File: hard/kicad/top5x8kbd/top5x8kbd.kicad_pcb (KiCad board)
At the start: 2 copper layers, 177.8 x 130.8 mm, 77 parts, among them J1 EXPANSION, J2 TO COMPUTER, J23 DB9_Male, J44 DB9_Male, J5 TO COMPUTER (DIRECT), SW1 1 !, SW10 0 _, SW11 Q ¡, SW12 W ~~, SW13 E é, SW14 R <, SW15 T >, SW16 Y ü, SW17 U ú, SW18 I í, SW19 O ó, SW2 2 @, SW20 P ", SW21 A á, SW22 S ;, SW23 D |, SW24 F [, SW25 G ], SW26 H ^, SW27 J -, SW28 K +, SW29 L =, SW3 3 #, SW30 ENTER ñ, SW31 SHIFT, SW32 Z :, SW33 X ¿, SW34 C ?, SW35 V /, SW36 B *, SW37 N ,, SW38 M ., SW39 ALT, SW4 4 $, SW40 SPACE, SW5 5 %, SW6 6 &, SW7 7 ', SW8 8 (, SW9 9 (, U1 74HC138, U12 74HC174, U13 74HC245, U24 74HC245, U26 74HC174, U34 74HC595, U45 74HC245, U55 74HC595, U9 74HC86

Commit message: add Sinclair keyboard headers
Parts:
- added J16: COLUMN, Connector_PinSocket_2.54mm:PinSocket_1x05_P2.54mm_Vertical, F.Cu at (135.9, 80.0)
- added J17: ROW, Connector_PinSocket_2.54mm:PinSocket_1x08_P2.54mm_Vertical, F.Cu at (153.7, 80.0)
- H3, H4, H5, H6, H7, H8: value MountingHole -> (none)
- LOGO1, LOGO2, LOGO3: value Logo_Open_Hardware_Large -> (none)
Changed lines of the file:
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@@
     (tracks 0)
     (zones 0)
-    (modules 77)
+    (modules 79)
     (nets 50)
   )
@@
     (add_net ROW8)
   )
+  (module Connector_PinSocket_2.54mm:PinSocket_1x08_P2.54mm_Vertical (layer F.Cu)
+    (at 153.67 80.01 90)
+    (descr "Through hole straight socket strip, 1x08, 2.54mm pitch, single row (from Kicad 4.0.7), script generated")
+    (tags "Through hole socket strip THT 1x08 2.54mm single row")
+    (fp_text reference J17 (at 2.54 8.89 unlocked) (layer B.SilkS)
+      (effects (font (size 1 1) (thickness 0.15)) (justify mirror))
+    )
+    (fp_text value ROW (at 2.54 8.89 180) (layer F.Fab)
+      (effects (font (size 1 1) (thickness 0.15)))
+    )
+    (fp_text user %R (at 0 8.89) (layer F.Fab)
+      (effects (font (size 1 1) (thickness 0.15)))
+    )
+    (fp_line (start -1.8 19.55) (end -1.8 -1.8) (layer F.CrtYd) (width 0.05))
+    (fp_line (start 1.75 19.55) (end -1.8 19.55) (layer F.CrtYd) (width 0.05))
+    (fp_line (start 1.75 -1.8) (end 1.75 19.55) (layer F.CrtYd) (width 0.05))
+    (fp_line (start -1.8 -1.8) (end 1.75 -1.8) (layer F.CrtYd) (width 0.05))
+    (fp_line (start 0 -1.33) (end 1.33 -1.33) (layer F.SilkS) (width 0.12))
+    (fp_line (start 1.33 -1.33) (end 1.33 0) (layer F.SilkS) (width 0.12))
+    (fp_line (start 1.33 1.27) (end 1.33 19.11) (layer F.SilkS) (width 0.12))
+    (fp_line (start -1.33 19.11) (end 1.33 19.11) (layer F.SilkS) (width 0.12))
+    (fp_line (start -1.33 1.27) (end -1.33 19.11) (layer F.SilkS) (width 0.12))
+    (fp_line (start -1.33 1.27) (end 1.33 1.27) (layer F.SilkS) (width 0.12))
+    (fp_line (start -1.27 19.05) (end -1.27 -1.27) (layer F.Fab) (width 0.1))
+    (fp_line (start 1.27 19.05) (end -1.27 19.05) (layer F.Fab) (width 0.1))
+    (fp_line (start 1.27 -0.635) (end 1.27 19.05) (layer F.Fab) (width 0.1))
+    (fp_line (start 0.635 -1.27) (end 1.27 -0.635) (layer F.Fab) (width 0.1))
+    (fp_line (start -1.27 -1.27) (end 0.635 -1.27) (layer F.Fab) (width 0.1))
+    (pad 8 thru_hole oval (at 0 17.78 90) (size 1.7 1.7) (drill 1) (layers *.Cu *.Mask)
+      (net 14 ROW8))
+    (pad 7 thru_hole oval (at 0 15.24 90) (size 1.7 1.7) (drill 1) (layers *.Cu *.Mask)
+      (net 12 ROW7))
+    (pad 6 thru_hole oval (at 0 12.7 90) (size 1.7 1.7) (drill 1) (layers *.Cu *.Mask)
+      (net 13 ROW6))
+    (pad 5 thru_hole oval (at 0 10.16 90) (size 1.7 1.7) (drill 1) (layers *.Cu *.Mask)
+      (net 10 ROW5))
+    (pad 4 thru_hole oval (at 0 7.62 90) (size 1.7 1.7) (drill 1) (layers *.Cu *.Mask)
+      (net 11 ROW3))
+    (pad 3 thru_hole oval (at 0 5.08 90) (size 1.7 1.7) (drill 1) (layers *.Cu *.Mask)
+      (net 8 ROW4))
+    (pad 2 thru_hole oval (at 0 2.54 90) (size 1.7 1.7) (drill 1) (layers *.Cu *.Mask)
+      (net 9 ROW2))
+    (pad 1 thru_hole rect (at 0 0 90) (size 1.7 1.7) (drill 1) (layers *.Cu *.Mask)
+      (net 3 ROW1))
+    (model ${KISYS3DMOD}/Connector_PinSocket_2.54mm.3dshapes/PinSocket_1x08_P2.54mm_Vertical.wrl
+      (at (xyz 0 0 0))
+      (scale (xyz 1 1 1))
+      (rotate (xyz 0 0 0))
+    )
+  )
+  (module Connector_PinSocket_2.54mm:PinSocket_1x05_P2.54mm_Vertical (layer F.Cu)
+    (at 135.89 80.01 90)
+    (descr "Through hole straight socket strip, 1x05, 2.54mm pitch, single row (from Kicad 4.0.7), script generated")
+    (tags "Through hole socket strip THT 1x05 2.54mm single row")
+    (fp_text reference J16 (at 2.54 5.08 unlocked) (layer B.SilkS)
+      (effects (font (size 1 1) (thickness 0.15)) (justify mirror))
+    )
+    (fp_text value COLUMN (at 2.54 5.08) (layer F.Fab)
+      (effects (font (size 1 1) (thickness 0.15)))
+    )
+    (fp_text user %R (at 0 5.08) (layer F.Fab)
+      (effects (font (size 1 1) (thickness 0.15)))
+    )
+    (fp_line (start -1.8 11.9) (end -1.8 -1.8) (layer F.CrtYd) (width 0.05))
+    (fp_line (start 1.75 11.9) (end -1.8 11.9) (layer F.CrtYd) (width 0.05))
+    (fp_line (start 1.75 -1.8) (end 1.75 11.9) (layer F.CrtYd) (width 0.05))
+    (fp_line (start -1.8 -1.8) (end 1.75 -1.8) (layer F.CrtYd) (width 0.05))
+    (fp_line (start 0 -1.33) (end 1.33 -1.33) (layer F.SilkS) (width 0.12))
+    (fp_line (start 1.33 -1.33) (end 1.33 0) (layer F.SilkS) (width 0.12))
+    (fp_line (start 1.33 1.27) (end 1.33 11.49) (layer F.SilkS) (width 0.12))
+    (fp_line (start -1.33 11.49) (end 1.33 11.49) (layer F.SilkS) (width 0.12))
+    (fp_line (start -1.33 1.27) (end -1.33 11.49) (layer F.SilkS) (width 0.12))
+    (fp_line (start -1.33 1.27) (end 1.33 1.27) (layer F.SilkS) (width 0.12))
+    (fp_line (start -1.27 11.43) (end -1.27 -1.27) (layer F.Fab) (width 0.1))
+    (fp_line (start 1.27 11.43) (end -1.27 11.43) (layer F.Fab) (width 0.1))
+    (fp_line (start 1.27 -0.635) (end 1.27 11.43) (layer F.Fab) (width 0.1))
+    (fp_line (start 0.635 -1.27) (end 1.27 -0.635) (layer F.Fab) (width 0.1))
+    (fp_line (start -1.27 -1.27) (end 0.635 -1.27) (layer F.Fab) (width 0.1))
+    (pad 5 thru_hole oval (at 0 10.16 90) (size 1.7 1.7) (drill 1) (layers *.Cu *.Mask)
+      (net 7 COL5))
+    (pad 4 thru_hole oval (at 0 7.62 90) (size 1.7 1.7) (drill 1) (layers *.Cu *.Mask)
+      (net 6 COL4))
+    (pad 3 thru_hole oval (at 0 5.08 90) (size 1.7 1.7) (drill 1) (layers *.Cu *.Mask)
+      (net 5 COL3))
+    (pad 2 thru_hole oval (at 0 2.54 90) (size 1.7 1.7) (drill 1) (layers *.Cu *.Mask)
+      (net 4 COL2))
+    (pad 1 thru_hole rect (at 0 0 90) (size 1.7 1.7) (drill 1) (layers *.Cu *.Mask)
+      (net 2 COL1))
+    (model ${KISYS3DMOD}/Connector_PinSocket_2.54mm.3dshapes/PinSocket_1x05_P2.54mm_Vertical.wrl
+      (at (xyz 0 0 0))
+      (scale (xyz 1 1 1))
+      (rotate (xyz 0 0 0))
+    )
+  )
   (module Jumper:SolderJumper-3_P1.3mm_Open_RoundedPad1.0x1.5mm (layer F.Cu)
     (at 162.56 45.72)
@@
       (effects (font (size 1.524 1.524) (thickness 0.3)))
     )
-    (fp_text value Logo_Open_Hardware_Large (at 0.75 0) (layer F.SilkS) hide
+    (fp_text value " " (at 0.75 0) (layer F.SilkS) hide
       (effects (font (size 1.524 1.524) (thickness 0.3)))
     )
@@
       (effects (font (size 1.524 1.524) (thickness 0.3)))
     )
-    (fp_text value Logo_Open_Hardware_Large (at 0.75 0) (layer F.SilkS) hide
+    (fp_text value " " (at 0.75 0) (layer F.SilkS) hide
       (effects (font (size 1.524 1.524) (thickness 0.3)))
     )
@@
       (effects (font (size 1 1) (thickness 0.15)))
     )
-    (fp_text value Logo_Open_Hardware_Large (at 0.75 0) (layer F.Fab) hide
+    (fp_text value " " (at 0.75 0) (layer F.Fab) hide
       (effects (font (size 1 1) (thickness 0.15)))
     )
@@
       (effects (font (size 1 1) (thickness 0.15)))
     )
-    (fp_text value MountingHole (at 0 3.8) (layer F.Fab)
+    (fp_text value " " (at 0 3.8) (layer F.Fab)
       (effects (font (size 1 1) (thickness 0.15)))
     )
@@
       (effects (font (size 1 1) (thickness 0.15)))
     )
-    (fp_text value MountingHole (at 0 3.8) (layer F.Fab)
+    (fp_text value " " (at 0 3.8) (layer F.Fab)
       (effects (font (size 1 1) (thickness 0.15)))
     )
@@
       (effects (font (size 1 1) (thickness 0.15)))
     )
-    (fp_text value MountingHole (at 0 3.8) (layer F.Fab)
+    (fp_text value " " (at 0 3.8) (layer F.Fab)
       (effects (font (size 1 1) (thickness 0.15)))
     )
@@
       (effects (font (size 1 1) (thickness 0.15)))
     )
-    (fp_text value MountingHole (at 0 3.8) (layer F.Fab)
+    (fp_text value " " (at 0 3.8) (layer F.Fab)
       (effects (font (size 1 1) (thickness 0.15)))
     )
@@
       (effects (font (size 1 1) (thickness 0.15)))
     )
-    (fp_text value MountingHole (at 0 3.8) (layer F.Fab)
+    (fp_text value " " (at 0 3.8) (layer F.Fab)
       (effects (font (size 1 1) (thickness 0.15)))
     )
@@
       (effects (font (size 1 1) (thickness 0.15)))
     )
-    (fp_text value MountingHole (at 0 3.8) (layer F.Fab)
+    (fp_text value " " (at 0 3.8) (layer F.Fab)
       (effects (font (size 1 1) (thickness 0.15)))
     )
@@
     (fp_line (start 6.25 -0.75) (end 6.25 5.25) (layer F.Fab) (width 0.1))
     (fp_line (start 3.25 -0.75) (end 6.25 -0.75) (layer F.Fab) (width 0.1))
-    (fp_text user %R (at 3.25 2.25) (layer F.Fab)
-      (effects (font (size 1 1) (thickness 0.15)))
-    )
+    (fp_text user BREAK (at 3.175 8.89) (layer F.SilkS)
+      (effects (font (size 1 1) (thickness 0.15)))
+    )

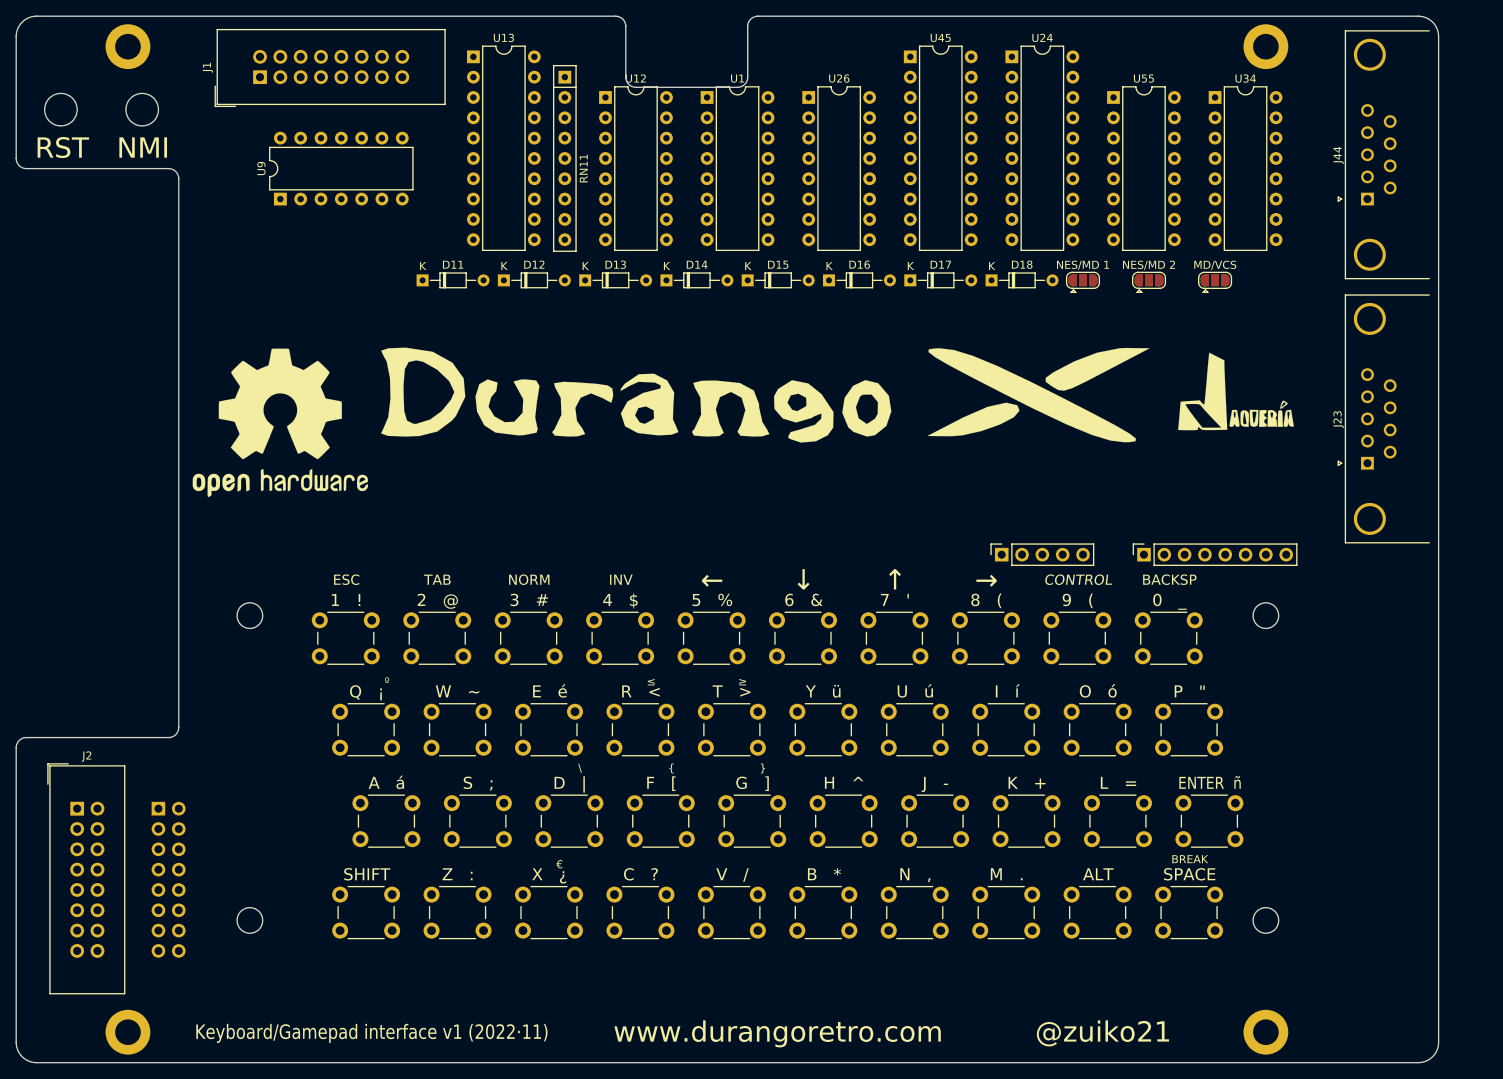
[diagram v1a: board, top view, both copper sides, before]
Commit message: fix cover edge cuts
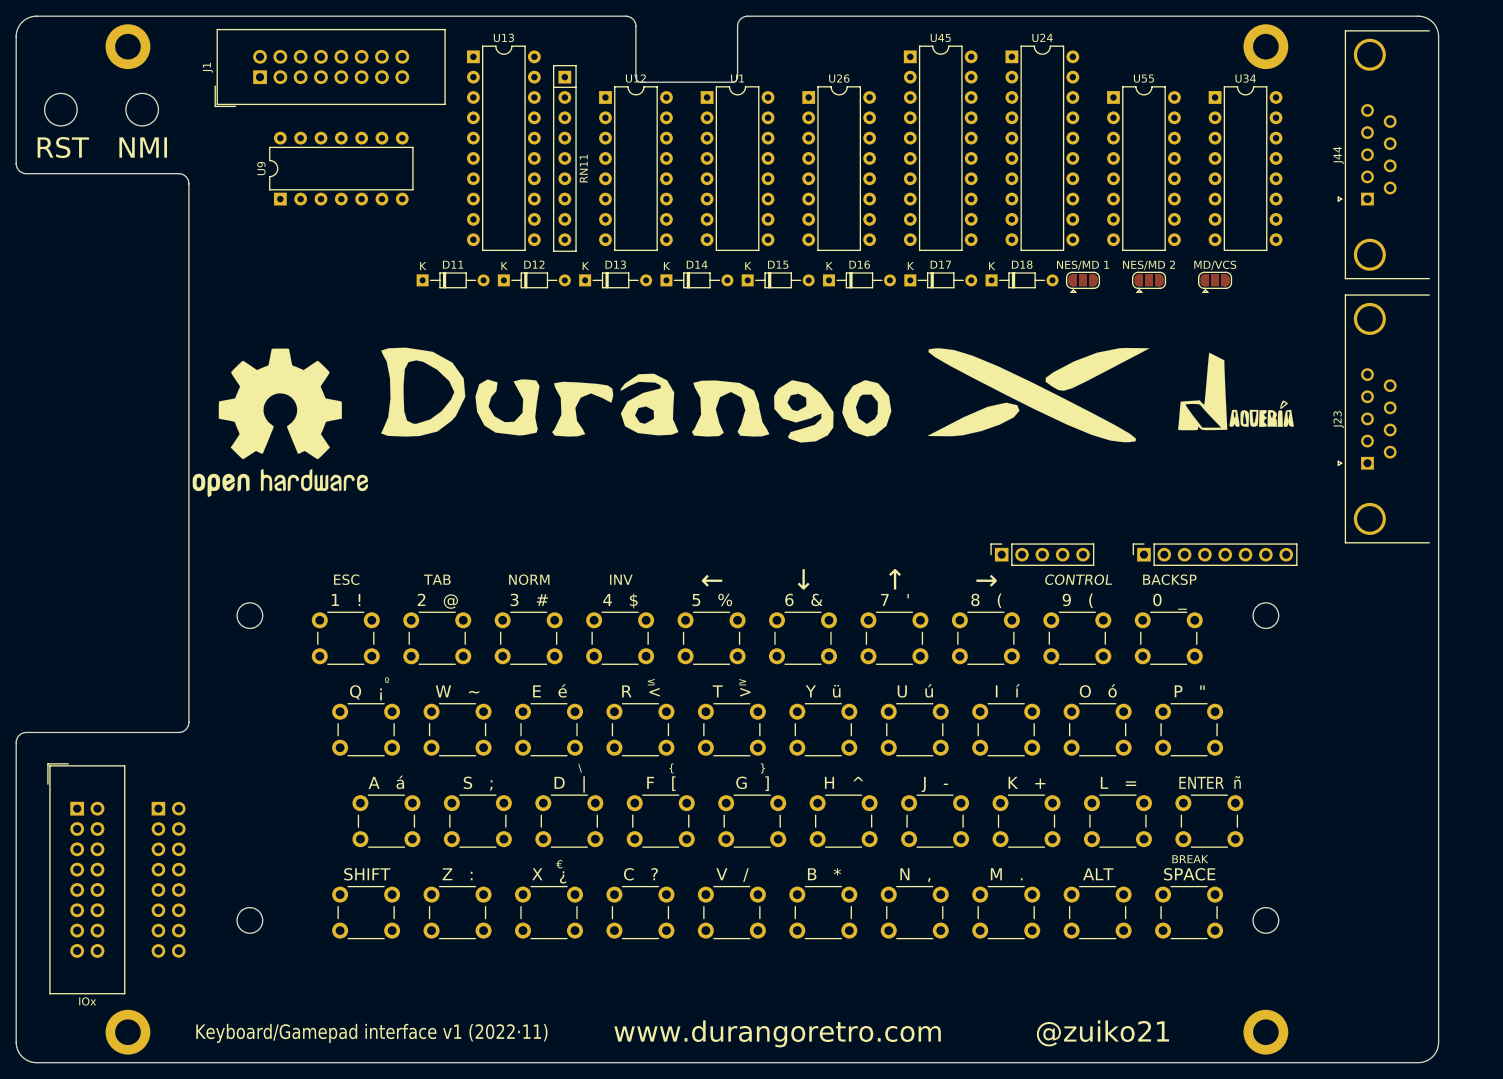
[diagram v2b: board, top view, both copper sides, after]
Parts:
- J1: value EXPANSION -> IOx
- J2: value TO COMPUTER -> IOx
- J5: value TO COMPUTER (DIRECT) -> TO COMPUTER
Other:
- outline, holes or cut-outs redrawn
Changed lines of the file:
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@@
       (effects (font (size 1 1) (thickness 0.15)) (justify mirror))
     )
-    (fp_text value "TO COMPUTER (DIRECT)" (at -1.27 -20.55) (layer B.Fab)
-      (effects (font (size 1 1) (thickness 0.15)) (justify mirror))
-    )
-    (fp_text user %R (at -1.27 -8.89 270) (layer B.Fab)
+    (fp_text value "TO COMPUTER" (at -1.27 -20.55 unlocked) (layer B.SilkS)
       (effects (font (size 1 1) (thickness 0.15)) (justify mirror))
     )
@@
     (descr "Through hole straight IDC box header, 2x08, 2.54mm pitch, double rows")
     (tags "Through hole IDC box header THT 2x08 2.54mm double row")
-    (fp_text reference J2 (at 1.27 -6.604) (layer F.SilkS)
-      (effects (font (size 1 1) (thickness 0.15)))
+    (fp_text reference J2 (at 1.27 -1.905 unlocked) (layer B.SilkS)
+      (effects (font (size 1 1) (thickness 0.15)) (justify mirror))
     )
-    (fp_text value "TO COMPUTER" (at 1.27 24.384) (layer F.Fab)
+    (fp_text value IOx (at 1.27 24.13 unlocked) (layer F.SilkS)
       (effects (font (size 1 1) (thickness 0.15)))
     )
@@
     (fp_line (start 5.145 -4.56) (end 5.145 22.32) (layer F.Fab) (width 0.1))
     (fp_line (start 5.695 -5.1) (end 5.695 22.88) (layer F.Fab) (width 0.1))
-    (fp_text user %R (at 1.27 8.89) (layer F.Fab)
-      (effects (font (size 1 1) (thickness 0.15)))
-    )
     (pad 16 thru_hole oval (at 2.54 17.78) (size 1.7272 1.7272) (drill 1.016) (layers *.Cu *.Mask)
       (net 15 PD7))
@@
       (effects (font (size 1 1) (thickness 0.15)))
     )
-    (fp_text value EXPANSION (at 1.27 24.384 90) (layer F.Fab)
+    (fp_text value IOx (at 1.27 24.384 90) (layer F.Fab)
       (effects (font (size 1 1) (thickness 0.15)))
     )
@@
     )
   )
+  (gr_arc (start 102.235 20.32) (end 102.235 20.955) (angle -90) (layer Edge.Cuts) (width 0.05))
+  (gr_arc (start 90.805 20.32) (end 90.17 20.32) (angle -90) (layer Edge.Cuts) (width 0.05))
   (gr_text @zuiko21 (at 148.59 139.7) (layer F.SilkS)
     (effects (font (size 2.54 2.54) (thickness 0.45)))
@@
     (effects (font (size 2.54 2.54) (thickness 0.3)))
   )
-  (gr_line (start 88.9 13.97) (end 88.9 20.32) (layer Edge.Cuts) (width 0.05))
-  (gr_arc (start 105.41 13.97) (end 105.41 12.7) (angle -90) (layer Edge.Cuts) (width 0.05))
-  (gr_arc (start 102.87 20.32) (end 102.87 21.59) (angle -90) (layer Edge.Cuts) (width 0.05))
-  (gr_arc (start 90.17 20.32) (end 88.9 20.32) (angle -90) (layer Edge.Cuts) (width 0.05))
-  (gr_line (start 105.41 12.7) (end 187.96 12.7) (layer Edge.Cuts) (width 0.05))
-  (gr_line (start 104.14 20.32) (end 104.14 13.97) (layer Edge.Cuts) (width 0.05))
-  (gr_line (start 90.17 21.59) (end 102.87 21.59) (layer Edge.Cuts) (width 0.05))
-  (gr_arc (start 87.63 13.97) (end 88.9 13.97) (angle -90) (layer Edge.Cuts) (width 0.05))
+  (gr_line (start 90.17 13.97) (end 90.17 20.32) (layer Edge.Cuts) (width 0.05))
+  (gr_arc (start 104.14 13.97) (end 104.14 12.7) (angle -90) (layer Edge.Cuts) (width 0.05))
+  (gr_line (start 104.14 12.7) (end 187.96 12.7) (layer Edge.Cuts) (width 0.05))
+  (gr_line (start 102.87 20.32) (end 102.87 13.97) (layer Edge.Cuts) (width 0.05))
+  (gr_line (start 90.805 20.955) (end 102.235 20.955) (layer Edge.Cuts) (width 0.05))
+  (gr_arc (start 88.9 13.97) (end 90.17 13.97) (angle -90) (layer Edge.Cuts) (width 0.05))
   (gr_circle (center 28.448 24.384) (end 30.48 24.384) (layer Edge.Cuts) (width 0.12))
   (gr_circle (center 18.288 24.384) (end 20.32 24.384) (layer Edge.Cuts) (width 0.12))
-  (gr_arc (start 13.97 104.14) (end 13.97 102.87) (angle -90) (layer Edge.Cuts) (width 0.05))
-  (gr_arc (start 31.75 101.6) (end 31.75 102.87) (angle -90) (layer Edge.Cuts) (width 0.05))
-  (gr_arc (start 31.75 33.02) (end 33.02 33.02) (angle -90) (layer Edge.Cuts) (width 0.05))
-  (gr_arc (start 13.97 30.48) (end 12.7 30.48) (angle -90) (layer Edge.Cuts) (width 0.05))
+  (gr_arc (start 13.97 103.505) (end 13.97 102.235) (angle -90) (layer Edge.Cuts) (width 0.05))
+  (gr_arc (start 33.02 100.965) (end 33.02 102.235) (angle -90) (layer Edge.Cuts) (width 0.05))
+  (gr_arc (start 33.02 33.655) (end 34.29 33.655) (angle -90) (layer Edge.Cuts) (width 0.05))
+  (gr_arc (start 13.97 31.115) (end 12.7 31.115) (angle -90) (layer Edge.Cuts) (width 0.05))
   (gr_arc (start 15.24 140.97) (end 12.7 140.97) (angle -90) (layer Edge.Cuts) (width 0.05))
   (gr_arc (start 187.96 140.97) (end 187.96 143.51) (angle -90) (layer Edge.Cuts) (width 0.05))
   (gr_arc (start 187.96 15.24) (end 190.5 15.24) (angle -90) (layer Edge.Cuts) (width 0.05))
   (gr_arc (start 15.24 15.24) (end 15.24 12.7) (angle -90) (layer Edge.Cuts) (width 0.05))
-  (gr_line (start 12.7 30.48) (end 12.7 15.24) (layer Edge.Cuts) (width 0.05))
-  (gr_line (start 31.75 31.75) (end 13.97 31.75) (layer Edge.Cuts) (width 0.05))
-  (gr_line (start 33.02 101.6) (end 33.02 33.02) (layer Edge.Cuts) (width 0.05))
-  (gr_line (start 13.97 102.87) (end 31.75 102.87) (layer Edge.Cuts) (width 0.05))
-  (gr_line (start 12.7 140.97) (end 12.7 104.14) (layer Edge.Cuts) (width 0.05))
+  (gr_line (start 12.7 31.115) (end 12.7 15.24) (layer Edge.Cuts) (width 0.05))
+  (gr_line (start 33.02 32.385) (end 13.97 32.385) (layer Edge.Cuts) (width 0.05))
+  (gr_line (start 34.29 100.965) (end 34.29 33.655) (layer Edge.Cuts) (width 0.05))
+  (gr_line (start 13.97 102.235) (end 33.02 102.235) (layer Edge.Cuts) (width 0.05))
+  (gr_line (start 12.7 140.97) (end 12.7 103.505) (layer Edge.Cuts) (width 0.05))
   (gr_line (start 187.96 143.51) (end 15.24 143.51) (layer Edge.Cuts) (width 0.05))
   (gr_line (start 190.5 15.24) (end 190.5 140.97) (layer Edge.Cuts) (width 0.05))
-  (gr_line (start 15.24 12.7) (end 87.63 12.7) (layer Edge.Cuts) (width 0.05))
+  (gr_line (start 15.24 12.7) (end 88.9 12.7) (layer Edge.Cuts) (width 0.05))
 )

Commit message: improve silkmask
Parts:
- J23: value DB9_Male -> MD/VCS1
- J44: value DB9_Male -> MD/VCS2
- RN11: value 22K -> 10K
- SW30: value ENTER ñ -> ENTER ñ
- moved LOGO3 10.8 mm to (165.7, 70.5)
- moved LOGO2 8.82 mm to (115.6, 55.2)
- moved LOGO1 4.02 mm to (47.0, 67.3)
- moved J23 1.27 mm to (181.6, 69.8)
- moved J44 1.27 mm to (181.6, 36.8)
